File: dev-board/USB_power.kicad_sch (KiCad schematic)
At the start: 10 parts, among them J4 TYPE-C-31-M12_13, J5 JST-4-pin, U2 TPD4E05U06DQAR, U3 BQ25606J

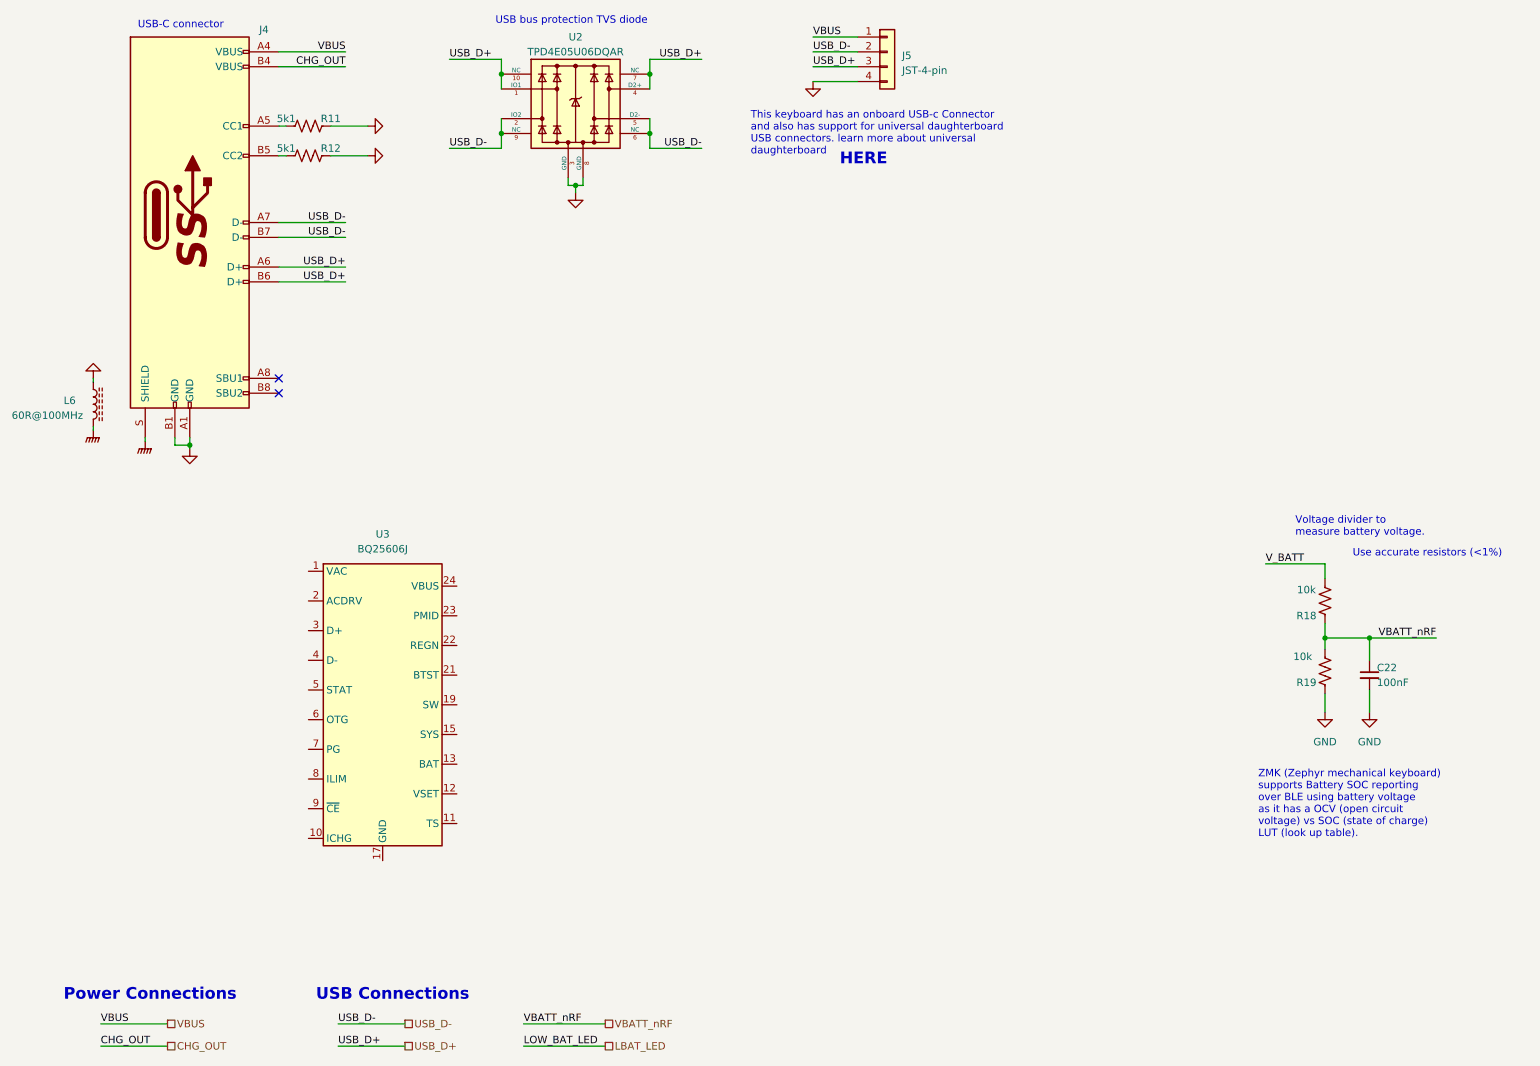
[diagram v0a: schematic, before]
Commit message: created dev-board to prove design before full-size
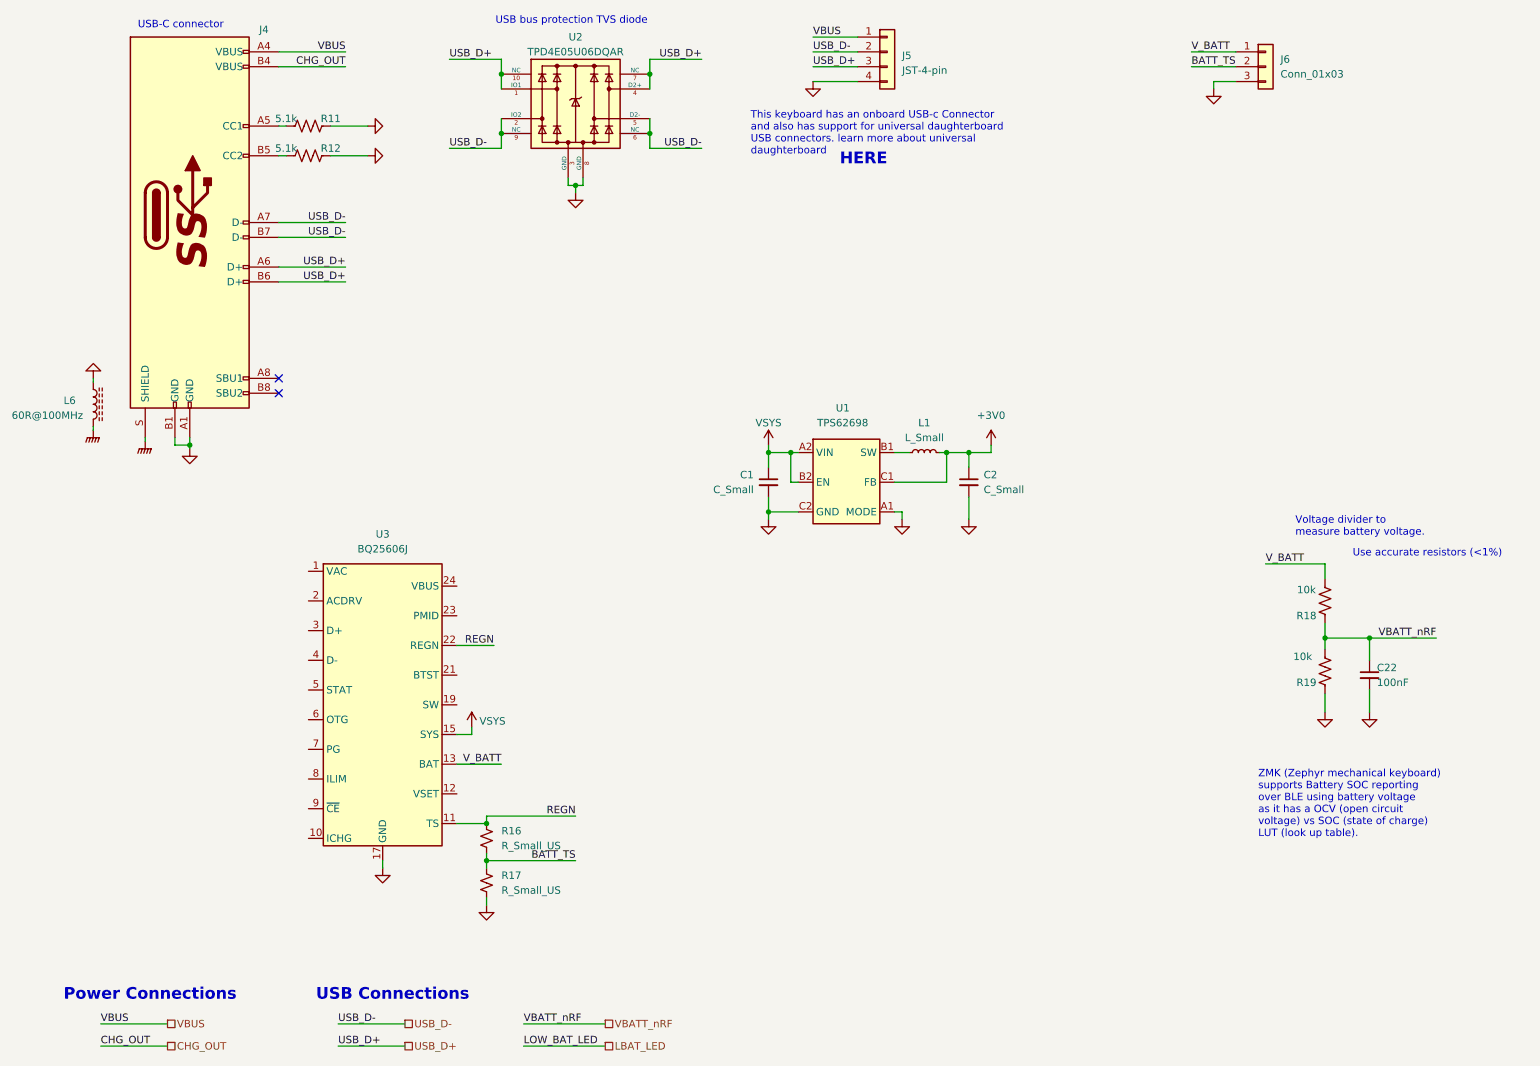
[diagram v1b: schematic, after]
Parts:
- added C1, C2: C_Small, keyboard:C_0402_1005Metric, symbol keyboard:C_Small
- added J6: Conn_01x03, symbol Connector_Generic:Conn_01x03
- added L1: L_Small, symbol Device:L_Small
- added R16, R17: R_Small_US, symbol Device:R_Small_US
- added U1: TPS62698, Package_BGA:Texas_DSBGA-6_0.9x1.4mm_Layout2x3_P0.5mm, symbol keyboard:TPS62698
- R11, R12: value 5k1 -> 5.1k
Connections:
- net V_BATT is gone; now on net BAT: R18.2
- net BAT: now also J6.1 (Pin_1)
- net GND: now also U3.17 (GND), U3.18 (GND), U3.25 (GND), C1.2, C2.2, J6.3 (Pin_3), R17.1, U1.A1 (MODE), U1.C2 (GND)
- net REGN: now reaches U3.11 (TS)
- net REGN: now also U3.22 (REGN), R16.2
- net VSYS: now reaches U3.15 (SYS), U3.16 (SYS)
- net VSYS: now also C1.1, U1.A2 (VIN), U1.B2 (EN)
- new net: L1.1, U1.B1 (SW)
- new net +3V0: C2.1, L1.2, U1.C1 (FB)
- new net BATT_TS: J6.2 (Pin_2), R16.1, R17.2

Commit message: battery charger components
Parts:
- added C3, C7, C8: 10uF, keyboard:C_0402_1005Metric, symbol keyboard:C_Small
- added C4: 1uF, keyboard:C_0402_1005Metric, symbol keyboard:C_Small
- added C5: 47nF, keyboard:C_0402_1005Metric, symbol keyboard:C_Small
- added C6: 4.7uF, keyboard:C_0402_1005Metric, symbol keyboard:C_Small
- added L2: 1uH, symbol Device:L_Small
- added R24, R28: 0, Resistor_SMD:R_0402_1005Metric, symbol Device:R_Small_US
- added R31: 0, symbol Device:R_Small_US
- added R32, R35: ??, keyboard:R_0402_1005Metric, symbol Device:R_Small_US
- added R33, R34: 10k, keyboard:R_0402_1005Metric, symbol Device:R_Small_US
- added R36: 0, keyboard:R_0402_1005Metric, symbol Device:R_Small_US
- added TP1, TP2: TestPoint, symbol Connector:TestPoint
- R16: value R_Small_US -> 5.23k; footprint (none) -> keyboard:R_0402_1005Metric
- R17: value R_Small_US -> 30.9k; footprint (none) -> keyboard:R_0402_1005Metric
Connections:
- net BAT: now also C3.1
- net GND: now also C3.2, C4.2, C6.2, C7.2, C8.2, R31.1, R32.2, R35.2, R36.2
- net USB_D+: now also R24.2
- net USB_D-: now also R28.2
- net VBUS: now also U3.1 (VAC), U3.24 (VBUS), C4.1
- net VSYS: now also C7.1, L2.2, R33.2, R34.2
- net at U3.10 (ICHG): now also R35.1
- net at U3.12 (VSET): now also R31.2
- net at U3.19 (SW), U3.20 (SW): now also C5.2, L2.1
- net at U3.21 (BTST): now also C5.1
- net at U3.23 (PMID): now also C8.1
- net at U3.3 (D+): now also R24.1
- net at U3.4 (D-): now also R28.1
- net at U3.5 (STAT): now also R34.1, TP1.1
- net OTG: now reaches U3.6 (OTG)
- net at U3.7 (PG): now also R33.1, TP2.1
- net at U3.8 (ILIM): now also R32.1
- net at U3.9 (~{CE}): now also R36.1
- net REGN: no longer names the net of R16.2, U3.11 (TS)
- net REGN: no longer U3.22 (REGN)
- new net: C6.1, U3.22 (REGN)
- no-connect marks 2 -> 3
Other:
- note added: "3.0V Buck Regulator"
- note added: "Battery Charger w/ Power Path"
- note added: "Battery Header"
- note added: "Resistors create 0-60C battery charging window."
